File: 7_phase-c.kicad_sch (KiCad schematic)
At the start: 28 parts, among them Q401 BSC072N08NS5, Q402 BSC072N08NS5, U401 IR2181S, U402 AD8418

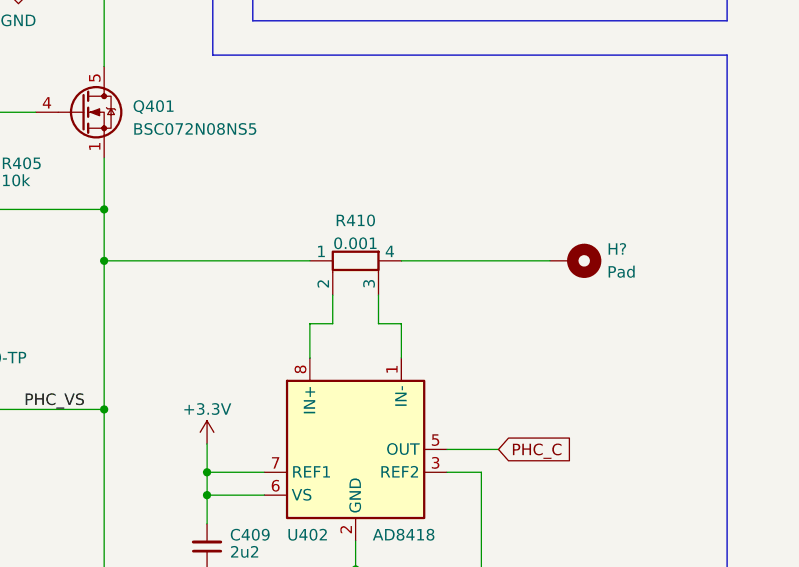
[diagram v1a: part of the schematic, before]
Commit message: feat: footprint assignment, circuit check and routing kickoff
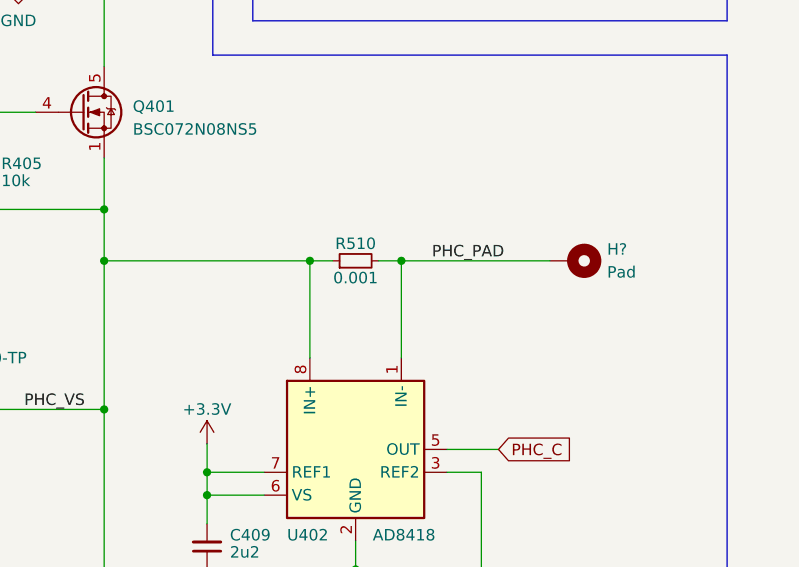
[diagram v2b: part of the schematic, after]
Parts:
- removed R410: 0.001, Resistor_SMD:R_2512_6332Metric, symbol Device:R_Shunt
- added R510: 0.001, Resistor_SMD:R_1206_3216Metric_Pad1.30x1.75mm_HandSolder, symbol Device:R_Small
- C410: footprint Capacitor_SMD:C_0402_1005Metric_Pad0.74x0.62mm_HandSolder -> Capacitor_SMD:C_0603_1608Metric_Pad1.08x0.95mm_HandSolder
- D401: Link (none) -> https://www.digikey.de/en/products/detail/rohm-semiconducto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
- D402: Link (none) -> https://www.digikey.de/en/products/detail/micro-commercial-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
- H?: footprint (none) -> TestPoint:TestPoint_THTPad_4.0x4.0mm_Drill2.0mm
- Q401, Q402: Link (none) -> https://www.digikey.de/en/products/detail/infineon-technolo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
- R408, R409: footprint Resistor_SMD:R_0402_1005Metric_Pad0.72x0.64mm_HandSolder -> Resistor_SMD:R_0603_1608Metric_Pad0.98x0.95mm_HandSolder
- U402: Link (none) -> https://www.digikey.de/en/products/detail/analog-devices-in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
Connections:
- net PHC_VS: now also U402.8 (IN+), R510.1
- net PHC_PAD: now reaches H?.1
- net PHC_PAD: now also U402.1 (IN-), R510.2
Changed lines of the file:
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@@
   (title_block
     (title "3-Phase Bridge - Phase C")
-    (date "2023-11-25")
+    (date "2023-11-26")
     (rev "1.0")
   )
@@
   (junction (at 250.19 35.56) (diameter 0) (color 0 0 0 0)
   )
+  (junction (at 244.475 83.185) (diameter 0) (color 0 0 0 0)
+  )
   (junction (at 198.755 66.675) (diameter 0) (color 0 0 0 0)
   )
@@
   (junction (at 201.93 40.005) (diameter 0) (color 0 0 0 0)
   )
-  (wire (pts (xy 236.855 90.17) (xy 236.855 86.995))
-    (stroke (width 0) (type default))
+  (junction (at 234.315 83.185) (diameter 0) (color 0 0 0 0)
   )
   (wire (pts (xy 42.545 95.885) (xy 47.625 95.885))
@@
     (stroke (width 0) (type default))
   )
-  (wire (pts (xy 241.935 86.995) (xy 241.935 90.17))
-    (stroke (width 0) (type default))
-  )
   (wire (pts (xy 191.77 48.895) (xy 191.77 52.07))
     (stroke (width 0) (type default))
@@
     (stroke (width 0) (type default))
   )
-  (wire (pts (xy 241.935 90.17) (xy 244.475 90.17))
-    (stroke (width 0) (type default))
-  )
   (wire (pts (xy 77.47 73.66) (xy 77.47 76.2))
     (stroke (width 0) (type default))
   )
-  (wire (pts (xy 234.315 90.17) (xy 236.855 90.17))
-    (stroke (width 0) (type default))
-  )
   (polyline (pts (xy 223.52 60.325) (xy 223.52 20.955))
     (stroke (width 0) (type default))
@@
     (stroke (width 0) (type default))
   )
-  (wire (pts (xy 234.315 93.98) (xy 234.315 90.17))
-    (stroke (width 0) (type default))
-  )
   (wire (pts (xy 198.755 66.675) (xy 203.835 66.675))
     (stroke (width 0) (type default))
@@
     (stroke (width 0) (type default))
   )
+  (wire (pts (xy 241.935 83.185) (xy 244.475 83.185))
+    (stroke (width 0) (type default))
+  )
   (wire (pts (xy 239.395 117.475) (xy 239.395 120.015))
     (stroke (width 0) (type default))
@@
     (stroke (width 0) (type default))
   )
+  (wire (pts (xy 234.315 83.185) (xy 234.315 93.98))
+    (stroke (width 0) (type default))
+  )
   (wire (pts (xy 244.475 83.185) (xy 260.985 83.185))
     (stroke (width 0) (type default))
@@
     (stroke (width 0) (type default))
   )
-  (wire (pts (xy 244.475 90.17) (xy 244.475 93.98))
-    (stroke (width 0) (type default))
-  )
   (polyline (pts (xy 223.52 20.955) (xy 148.59 20.955))
     (stroke (width 0) (type default))
   )
+  (wire (pts (xy 244.475 83.185) (xy 244.475 93.98))
+    (stroke (width 0) (type default))
+  )
   (wire (pts (xy 97.155 98.425) (xy 108.585 98.425))
     (stroke (width 0) (type default))
@@
   )
   (wire (pts (xy 114.935 66.04) (xy 114.935 71.755))
+    (stroke (width 0) (type default))
+  )
+  (wire (pts (xy 234.315 83.185) (xy 236.855 83.185))
     (stroke (width 0) (type default))
   )
@@
   (text "Half-Bridge Driver" (at 23.495 51.435 0)
     (effects (font (size 1.6 1.6) italic) (justify left bottom))
+  )
+  (label "PHC_PAD" (at 255.905 83.185 180) (fields_autoplaced)
+    (effects (font (size 1.27 1.27)) (justify right bottom))
   )
   (label "PHC_VS" (at 202.565 99.695 0) (fields_autoplaced)
@@
     )
   )
+  (symbol (lib_id "Device:R_Small") (at 239.395 83.185 90) (unit 1)
+    (in_bom yes) (on_board yes) (dnp no)
+    (property "Reference" "R510" (at 239.395 81.28 90)
+      (effects (font (size 1.27 1.27)))
+    )
+    (property "Value" "0.001" (at 239.395 85.09 90)
+      (effects (font (size 1.27 1.27)))
+    )
+    (property "Footprint" "Resistor_SMD:R_1206_3216Metric_Pad1.30x1.75mm_HandSolder" (at 239.395 83.185 0)
+      (effects (font (size 1.27 1.27)) hide)
+    )
+    (property "Datasheet" "~" (at 239.395 83.185 0)
+      (effects (font (size 1.27 1.27)) hide)
+    )
+    (pin "1")
+    (pin "2")
+    (instances
+      (project "ESC_R1"
+        (path "/9dea2e18-5867-4ed4-a12d-7ee109225de0/a82201a8-9dca-4a1d-828e-2de3fb3c1adb"
+          (reference "R510") (unit 1)
+        )
+        (path "/9dea2e18-5867-4ed4-a12d-7ee109225de0/912dc4da-f7bc-46bd-8800-06fc31d708dd"
+          (reference "R710") (unit 1)
+        )
+      )
+    )
+  )
   (symbol (lib_id "power:+BATT") (at 211.455 34.29 0) (unit 1)
     (in_bom yes) (on_board yes) (dnp no) (fields_autoplaced)
@@
       (effects (font (size 1.27 1.27)) hide)
     )
+    (property "Link" "https://www.digikey.de/en/products/detail/rohm-semiconductor/RB162MM-60TR/5001869" (at 114.935 74.295 0)
+      (effects (font (size 1.27 1.27)) hide)
+    )
     (pin "1")
     (pin "2")
@@
       (effects (font (size 1.27 1.27)) (justify right))
     )
-    (property "Footprint" "Capacitor_SMD:C_0402_1005Metric_Pad0.74x0.62mm_HandSolder" (at 250.19 41.275 0)
+    (property "Footprint" "Capacitor_SMD:C_0603_1608Metric_Pad1.08x0.95mm_HandSolder" (at 250.19 41.275 0)
       (effects (font (size 1.27 1.27)) hide)
     )
@@
       (effects (font (size 1.27 1.27)) (justify left))
     )
-    (property "Footprint" "Resistor_SMD:R_0402_1005Metric_Pad0.72x0.64mm_HandSolder" (at 184.785 105.41 0)
+    (property "Footprint" "Resistor_SMD:R_0603_1608Metric_Pad0.98x0.95mm_HandSolder" (at 184.785 105.41 0)
       (effects (font (size 1.27 1.27)) hide)
     )
@@
       (effects (font (size 1.27 1.27)) (justify left) hide)
     )
+    (property "Link" "https://www.digikey.de/en/products/detail/infineon-technologies/BSC072N08NS5ATMA1/5959908" (at 208.915 66.675 0)
+      (effects (font (size 1.27 1.27)) hide)
+    )
     (pin "1")
     (pin "2")
@@
       (effects (font (size 1.27 1.27)))
     )
-    (property "Footprint" "Resistor_SMD:R_0402_1005Metric_Pad0.72x0.64mm_HandSolder" (at 196.85 99.695 0)
+    (property "Footprint" "Resistor_SMD:R_0603_1608Metric_Pad0.98x0.95mm_HandSolder" (at 196.85 99.695 0)
       (effects (font (size 1.27 1.27)) hide)
     )
@@
       (effects (font (size 1.27 1.27)) (justify left))
     )
-    (property "Footprint" "" (at 263.525 83.185 0)
+    (property "Footprint" "TestPoint:TestPoint_THTPad_4.0x4.0mm_Drill2.0mm" (at 263.525 83.185 0)
       (effects (font (size 1.27 1.27)) hide)
     )
@@
         (path "/9dea2e18-5867-4ed4-a12d-7ee109225de0/912dc4da-f7bc-46bd-8800-06fc31d708dd"
           (reference "H701") (unit 1)
-        )
-      )
-    )
-  )
-  (symbol (lib_id "Device:R_Shunt") (at 239.395 83.185 90) (mirror x) (unit 1)
-    (in_bom yes) (on_board yes) (dnp no) (fields_autoplaced)
-    (property "Reference" "R410" (at 239.395 78.74 90)
-      (effects (font (size 1.27 1.27)))
-    )
-    (property "Value" "0.001" (at 239.395 81.28 90)
-      (effects (font (size 1.27 1.27)))
-    )
-    (property "Footprint" "Resistor_SMD:R_2512_6332Metric" (at 239.395 81.407 90)
-      (effects (font (size 1.27 1.27)) hide)
-    )
-    (property "Datasheet" "~" (at 239.395 83.185 0)
-      (effects (font (size 1.27 1.27)) hide)
-    )
-    (property "Link" "https://www.digikey.de/en/products/detail/bourns-inc/CSS2H-2512R-1L00F/6023764" (at 239.395 83.185 90)
-      (effects (font (size 1.27 1.27)) hide)
-    )
-    (pin "1")
-    (pin "2")
-    (pin "3")
-    (pin "4")
-    (instances
-      (project "ESC_R1"
-        (path "/9dea2e18-5867-4ed4-a12d-7ee109225de0/a82201a8-9dca-4a1d-828e-2de3fb3c1adb"
-          (reference "R410") (unit 1)
-        )
-        (path "/9dea2e18-5867-4ed4-a12d-7ee109225de0/c42edb1a-90dc-4d64-9c27-05abb4553a36"
-          (reference "R12") (unit 1)
-        )
-        (path "/9dea2e18-5867-4ed4-a12d-7ee109225de0/912dc4da-f7bc-46bd-8800-06fc31d708dd"
-          (reference "R710") (unit 1)
         )
       )
@@
       (effects (font (size 1.27 1.27)) (justify left) hide)
     )
+    (property "Link" "https://www.digikey.de/en/products/detail/infineon-technologies/BSC072N08NS5ATMA1/5959908" (at 208.915 133.35 0)
+      (effects (font (size 1.27 1.27)) hide)
+    )
     (pin "1")
     (pin "2")
@@
       (effects (font (size 1.27 1.27)) hide)
     )
+    (property "Link" "https://www.digikey.de/en/products/detail/micro-commercial-co/MBR0530-TP/717251" (at 189.865 92.71 0)
+      (effects (font (size 1.27 1.27)) hide)
+    )
     (pin "1")
     (pin "2")
@@
         )
         (path "/9dea2e18-5867-4ed4-a12d-7ee109225de0/912dc4da-f7bc-46bd-8800-06fc31d708dd"
-          (reference "D5") (unit 1)
+          (reference "D702") (unit 1)
         )
       )
@@
       (effects (font (size 1.27 1.27)) hide)
     )
+    (property "Link" "https://www.digikey.de/en/products/detail/analog-devices-inc/AD8418AWBRZ/4571735" (at 239.395 104.14 0)
+      (effects (font (size 1.27 1.27)) hide)
+    )

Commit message: feat: initial layout of phase C
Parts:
- C405: footprint Capacitor_SMD:C_0603_1608Metric_Pad1.08x0.95mm_HandSolder -> Capacitor_SMD:C_1206_3216Metric_Pad1.33x1.80mm_HandSolder
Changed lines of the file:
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@@
       (effects (font (size 1.27 1.27)) (justify left))
     )
-    (property "Footprint" "Capacitor_SMD:C_0603_1608Metric_Pad1.08x0.95mm_HandSolder" (at 114.935 88.9 0)
+    (property "Footprint" "Capacitor_SMD:C_1206_3216Metric_Pad1.33x1.80mm_HandSolder" (at 114.935 88.9 0)
       (effects (font (size 1.27 1.27)) hide)
     )

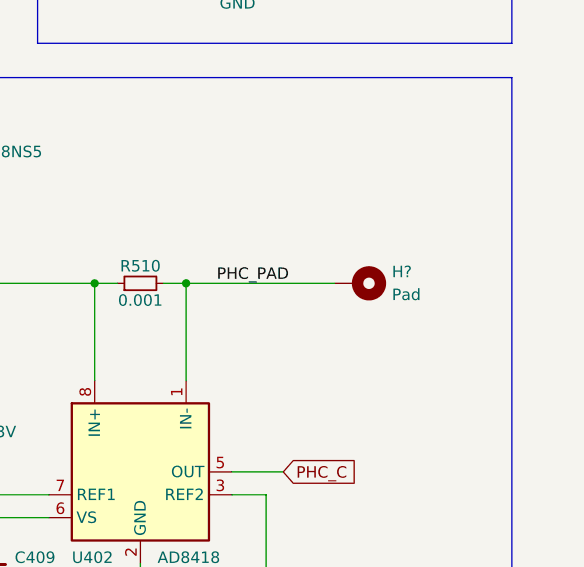
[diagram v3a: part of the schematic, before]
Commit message: feat: component placement for 1 phase completed
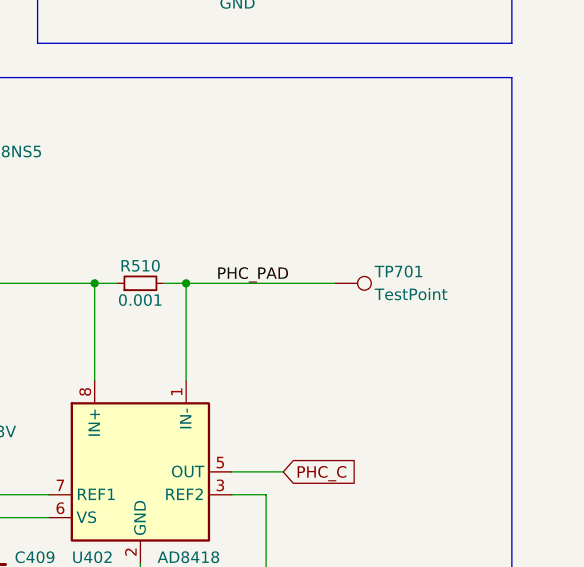
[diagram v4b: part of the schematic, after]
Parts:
- removed H?: Pad, TestPoint:TestPoint_THTPad_4.0x4.0mm_Drill2.0mm, symbol Mechanical:MountingHole_Pad
- added TP701: TestPoint, TestPoint:TestPoint_Pad_5.0x7.0mm, symbol Connector:TestPoint
- C405: footprint Capacitor_SMD:C_1206_3216Metric_Pad1.33x1.80mm_HandSolder -> Capacitor_SMD:C_0603_1608Metric_Pad1.08x0.95mm_HandSolder
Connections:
- net PHC_PAD: now also TP701.1
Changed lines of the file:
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@@
+    )
+  )
+  (symbol (lib_id "Connector:TestPoint") (at 260.985 83.185 270) (unit 1)
+    (in_bom yes) (on_board yes) (dnp no)
+    (property "Reference" "TP701" (at 265.43 81.915 90)
+      (effects (font (size 1.27 1.27)) (justify left))
+    )
+    (property "Value" "TestPoint" (at 265.43 84.455 90)
+      (effects (font (size 1.27 1.27)) (justify left))
+    )
+    (property "Footprint" "TestPoint:TestPoint_Pad_5.0x7.0mm" (at 260.985 88.265 0)
+      (effects (font (size 1.27 1.27)) hide)
+    )
+    (property "Datasheet" "~" (at 260.985 88.265 0)
+      (effects (font (size 1.27 1.27)) hide)
+    )
+    (pin "1")
+    (instances
+      (project "ESC_R1"
+        (path "/9dea2e18-5867-4ed4-a12d-7ee109225de0/912dc4da-f7bc-46bd-8800-06fc31d708dd"
+          (reference "TP701") (unit 1)
+        )
+      )
     )
   )
@@
         (path "/9dea2e18-5867-4ed4-a12d-7ee109225de0/912dc4da-f7bc-46bd-8800-06fc31d708dd"
           (reference "R708") (unit 1)
-        )
-      )
-    )
-  )
-  (symbol (lib_id "Mechanical:MountingHole_Pad") (at 263.525 83.185 270) (unit 1)
-    (in_bom yes) (on_board yes) (dnp no)
-    (property "Reference" "H?" (at 267.335 81.9149 90)
-      (effects (font (size 1.27 1.27)) (justify left))
-    )
-    (property "Value" "Pad" (at 267.335 84.455 90)
-      (effects (font (size 1.27 1.27)) (justify left))
-    )
-    (property "Footprint" "TestPoint:TestPoint_THTPad_4.0x4.0mm_Drill2.0mm" (at 263.525 83.185 0)
-      (effects (font (size 1.27 1.27)) hide)
-    )
-    (property "Datasheet" "~" (at 263.525 83.185 0)
-      (effects (font (size 1.27 1.27)) hide)
-    )
-    (pin "1")
-    (instances
-      (project "ESC_R1"
-        (path "/9dea2e18-5867-4ed4-a12d-7ee109225de0/a82201a8-9dca-4a1d-828e-2de3fb3c1adb"
-          (reference "H?") (unit 1)
-        )
-        (path "/9dea2e18-5867-4ed4-a12d-7ee109225de0/c42edb1a-90dc-4d64-9c27-05abb4553a36"
-          (reference "H1") (unit 1)
-        )
-        (path "/9dea2e18-5867-4ed4-a12d-7ee109225de0/912dc4da-f7bc-46bd-8800-06fc31d708dd"
-          (reference "H701") (unit 1)
         )
       )
@@
       (effects (font (size 1.27 1.27)) (justify left))
     )
-    (property "Footprint" "Capacitor_SMD:C_1206_3216Metric_Pad1.33x1.80mm_HandSolder" (at 114.935 88.9 0)
-      (effects (font (size 1.27 1.27)) hide)
-    )
+    (property "Footprint" "Capacitor_SMD:C_0603_1608Metric_Pad1.08x0.95mm_HandSolder" (at 114.935 88.9 0)
+      (effects (font (size 1.27 1.27)) hide)
+    )

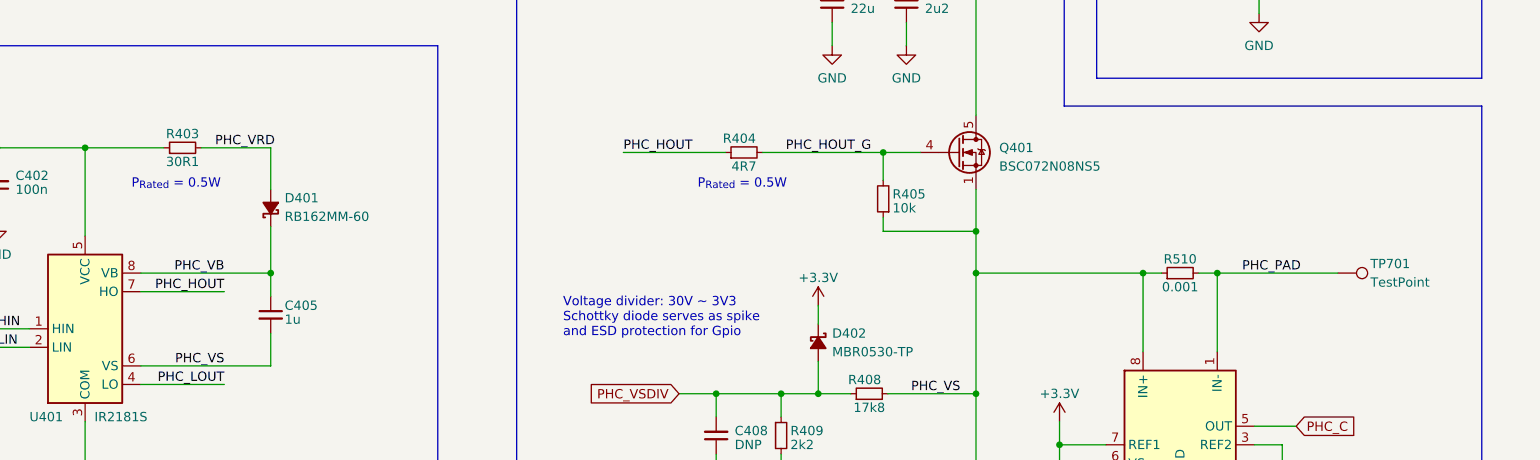
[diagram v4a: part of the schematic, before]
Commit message: fix: fixed LTSpice simulation and updated track widths accordingly
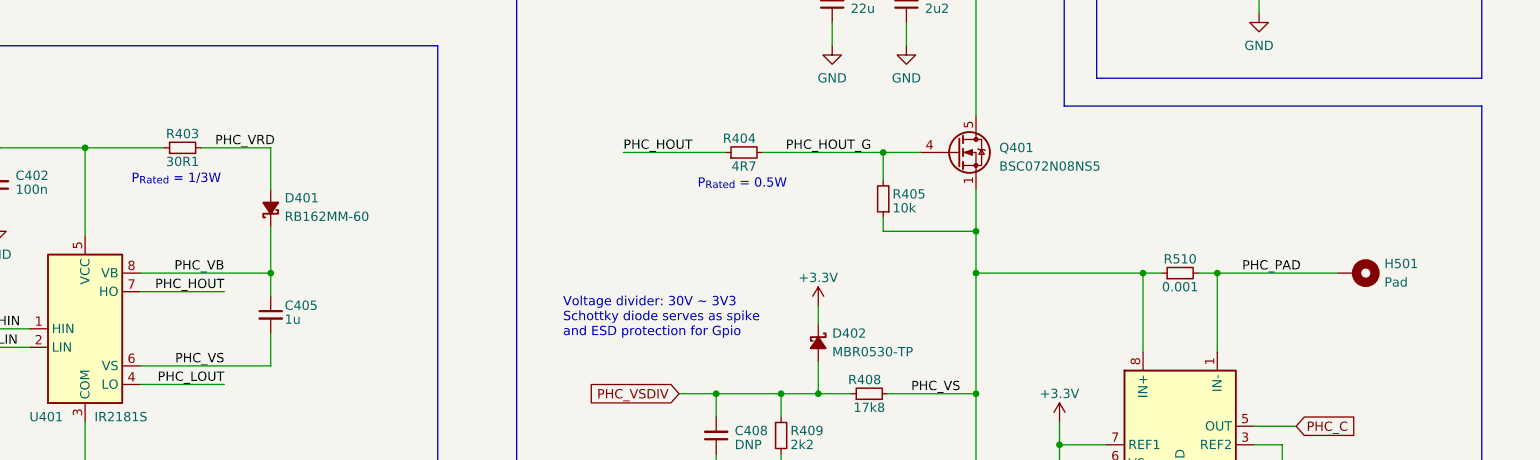
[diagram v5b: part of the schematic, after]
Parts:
- removed TP701: TestPoint, TestPoint:TestPoint_Pad_5.0x7.0mm, symbol Connector:TestPoint
- added H501: Pad, TestPoint:TestPoint_Pad_5.0x7.0mm, symbol Mechanical:MountingHole_Pad
- R403: Link (none) -> https://www.digikey.de/en/products/detail/vishay-dale/CRCW0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
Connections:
- net PHC_PAD: now also H501.1
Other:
- note added: "P_{Rated} = 1/3W"
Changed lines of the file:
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@@
     (effects (font (size 1.6 1.6) italic) (justify left bottom))
   )
-  (text "P_{Rated} = 0.5W\n" (at 95.885 71.755 0)
+  (text "P_{Rated} = 1/3W\n" (at 95.885 71.12 0)
     (effects (font (size 1.27 1.27)) (justify left bottom))
   )
@@
     )
   )
-  (symbol (lib_id "Connector:TestPoint") (at 260.985 83.185 270) (unit 1)
-    (in_bom yes) (on_board yes) (dnp no)
-    (property "Reference" "TP701" (at 265.43 81.915 90)
-      (effects (font (size 1.27 1.27)) (justify left))
-    )
-    (property "Value" "TestPoint" (at 265.43 84.455 90)
-      (effects (font (size 1.27 1.27)) (justify left))
-    )
-    (property "Footprint" "TestPoint:TestPoint_Pad_5.0x7.0mm" (at 260.985 88.265 0)
-      (effects (font (size 1.27 1.27)) hide)
-    )
-    (property "Datasheet" "~" (at 260.985 88.265 0)
-      (effects (font (size 1.27 1.27)) hide)
-    )
-    (pin "1")
-    (instances
-      (project "ESC_R1"
-        (path "/9dea2e18-5867-4ed4-a12d-7ee109225de0/912dc4da-f7bc-46bd-8800-06fc31d708dd"
-          (reference "TP701") (unit 1)
-        )
-      )
-    )
-  )
   (symbol (lib_id "power:GND") (at 66.04 109.22 0) (unit 1)
     (in_bom yes) (on_board yes) (dnp no)
@@
         (path "/9dea2e18-5867-4ed4-a12d-7ee109225de0/912dc4da-f7bc-46bd-8800-06fc31d708dd"
           (reference "R708") (unit 1)
+        )
+      )
+    )
+  )
+  (symbol (lib_id "Mechanical:MountingHole_Pad") (at 263.525 83.185 270) (unit 1)
+    (in_bom yes) (on_board yes) (dnp no)
+    (property "Reference" "H501" (at 267.335 81.9149 90)
+      (effects (font (size 1.27 1.27)) (justify left))
+    )
+    (property "Value" "Pad" (at 267.335 84.455 90)
+      (effects (font (size 1.27 1.27)) (justify left))
+    )
+    (property "Footprint" "TestPoint:TestPoint_Pad_5.0x7.0mm" (at 263.525 83.185 0)
+      (effects (font (size 1.27 1.27)) hide)
+    )
+    (property "Datasheet" "~" (at 263.525 83.185 0)
+      (effects (font (size 1.27 1.27)) hide)
+    )
+    (pin "1")
+    (instances
+      (project "ESC_R1"
+        (path "/9dea2e18-5867-4ed4-a12d-7ee109225de0/a82201a8-9dca-4a1d-828e-2de3fb3c1adb"
+          (reference "H501") (unit 1)
+        )
+        (path "/9dea2e18-5867-4ed4-a12d-7ee109225de0/912dc4da-f7bc-46bd-8800-06fc31d708dd"
+          (reference "H701") (unit 1)
         )
       )
@@
       (effects (font (size 1.27 1.27)) hide)
     )
+    (property "Link" "https://www.digikey.de/en/products/detail/vishay-dale/CRCW060333R0FKEAHP/2222237" (at 102.87 66.04 0)
+      (effects (font (size 1.27 1.27)) hide)
+    )
